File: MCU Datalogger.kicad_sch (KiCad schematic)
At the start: 25 parts, among them U1 24LC1025, U2 DS1337S_, U3 24LC1025, U4 ATMEGA328P-AU, Y1 32.768 kHZ, Y2 16 MHz

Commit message: Completed Comments
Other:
- note added: "EEPROM"
- note added: "MCU"
- note added: "Mounting"
- note added: "Real Time Clock"
- moved on the sheet: BT1, C2, C3, C4, C5, D1, D2, R5, R6, R7, U4, Y2

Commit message: Setup PCB-new
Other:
- company: N/A -> Mark Islam
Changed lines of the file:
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@@
 		(date "2026-09-06")
 		(rev "1")
-		(company "N/A")
+		(company "Mark Islam")
 	)
 	(text "Real Time Clock"

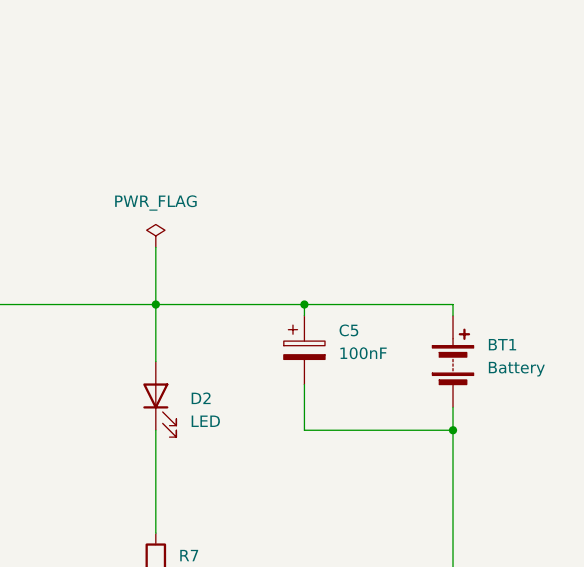
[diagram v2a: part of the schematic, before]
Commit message: Complete PCB Layout and DRC Check Complete
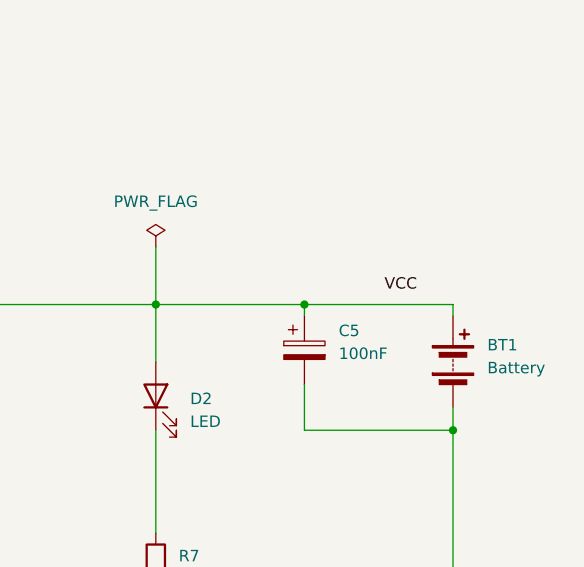
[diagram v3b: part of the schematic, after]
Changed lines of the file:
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@@
+		)
+	)
+	(label "VCC"
+		(at 264.16 34.29 0)
+		(effects
+			(font
+				(size 1.27 1.27)
+			)
+			(justify left bottom)
 		)
 	)
